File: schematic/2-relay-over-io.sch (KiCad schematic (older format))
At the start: 26 parts, among them J1 Screw_Terminal_01x03, J2 Screw_Terminal_01x03, J5 Conn_02x05_Odd_Even, J6 Conn_02x05_Odd_Even, J7 Conn_02x08_Odd_Even, J8 Conn_02x08_Odd_Even, Q2 BC817, Q3 BC817, U2 SONGLE_3V_relay, U3 SONGLE_3V_relay, U6 DizzyBITLogo, U7 DizzyBIT-Layout

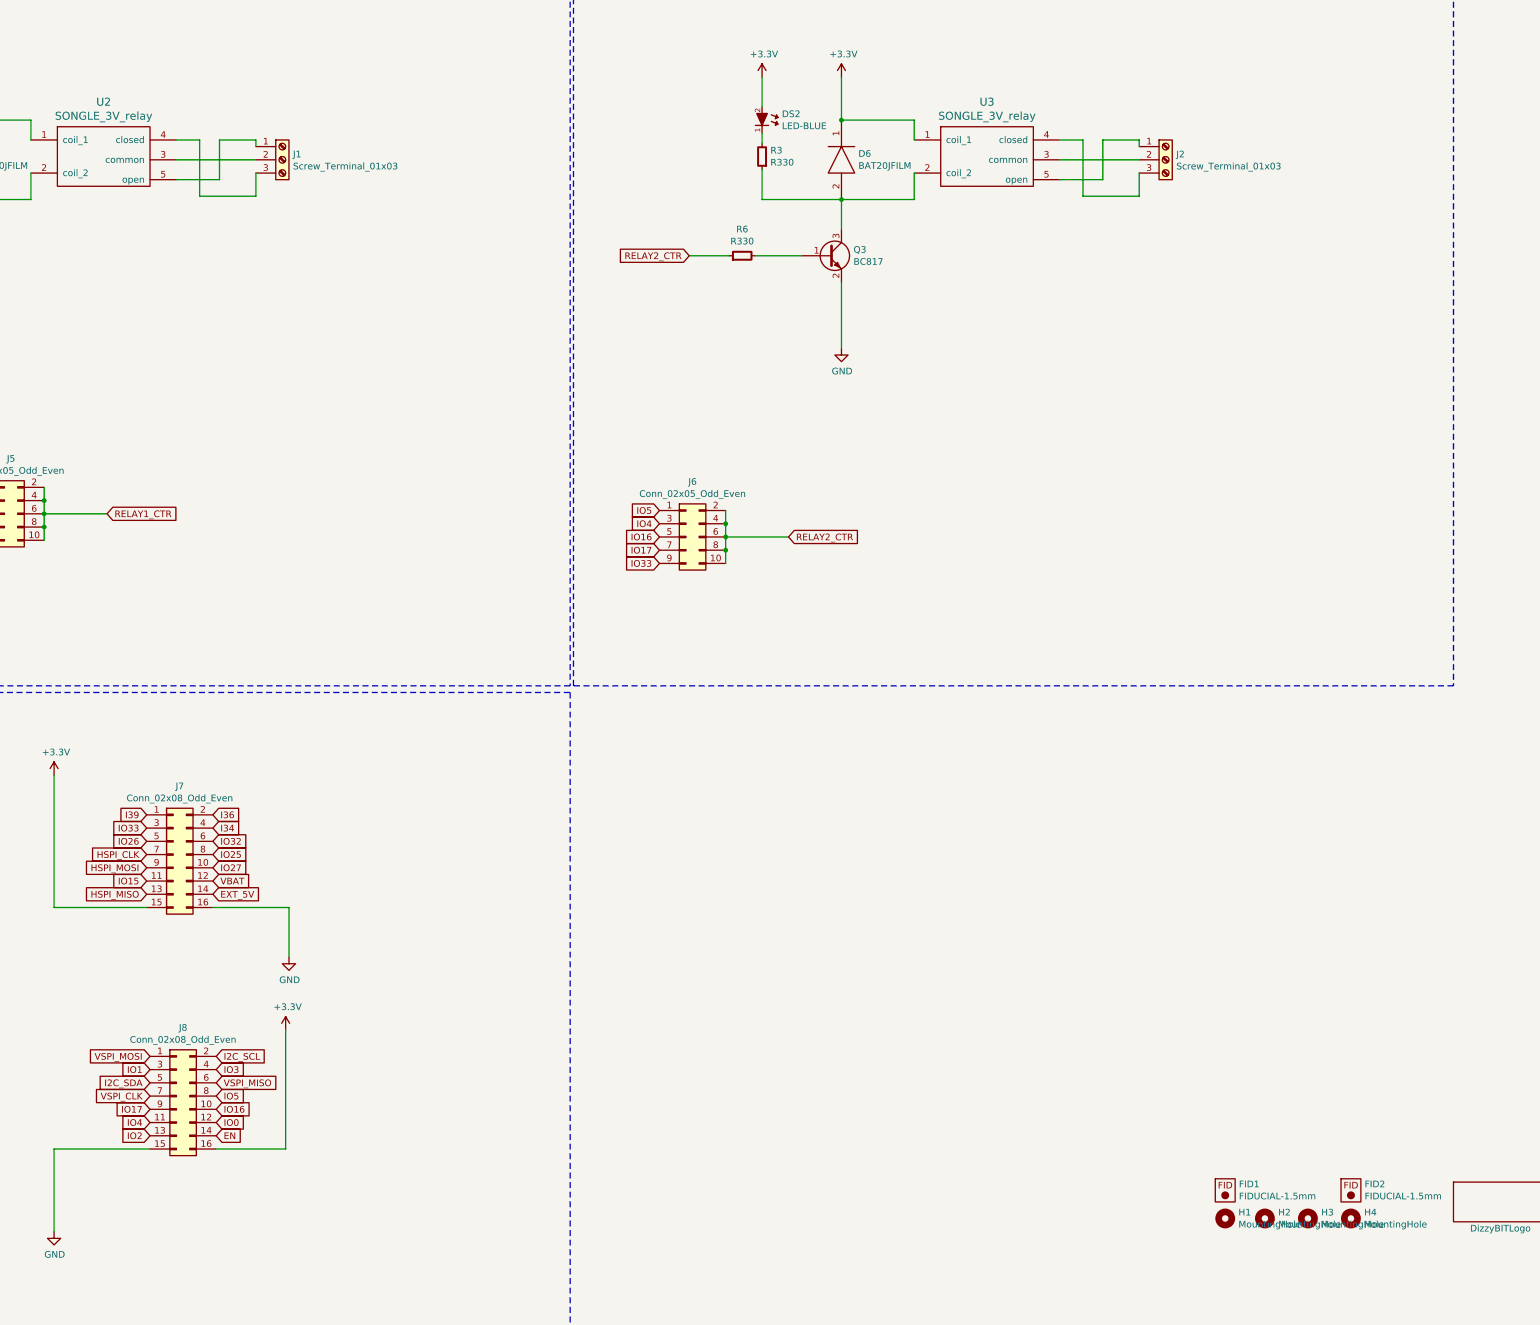
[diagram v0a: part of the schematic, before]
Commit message: Updated according to standard module design
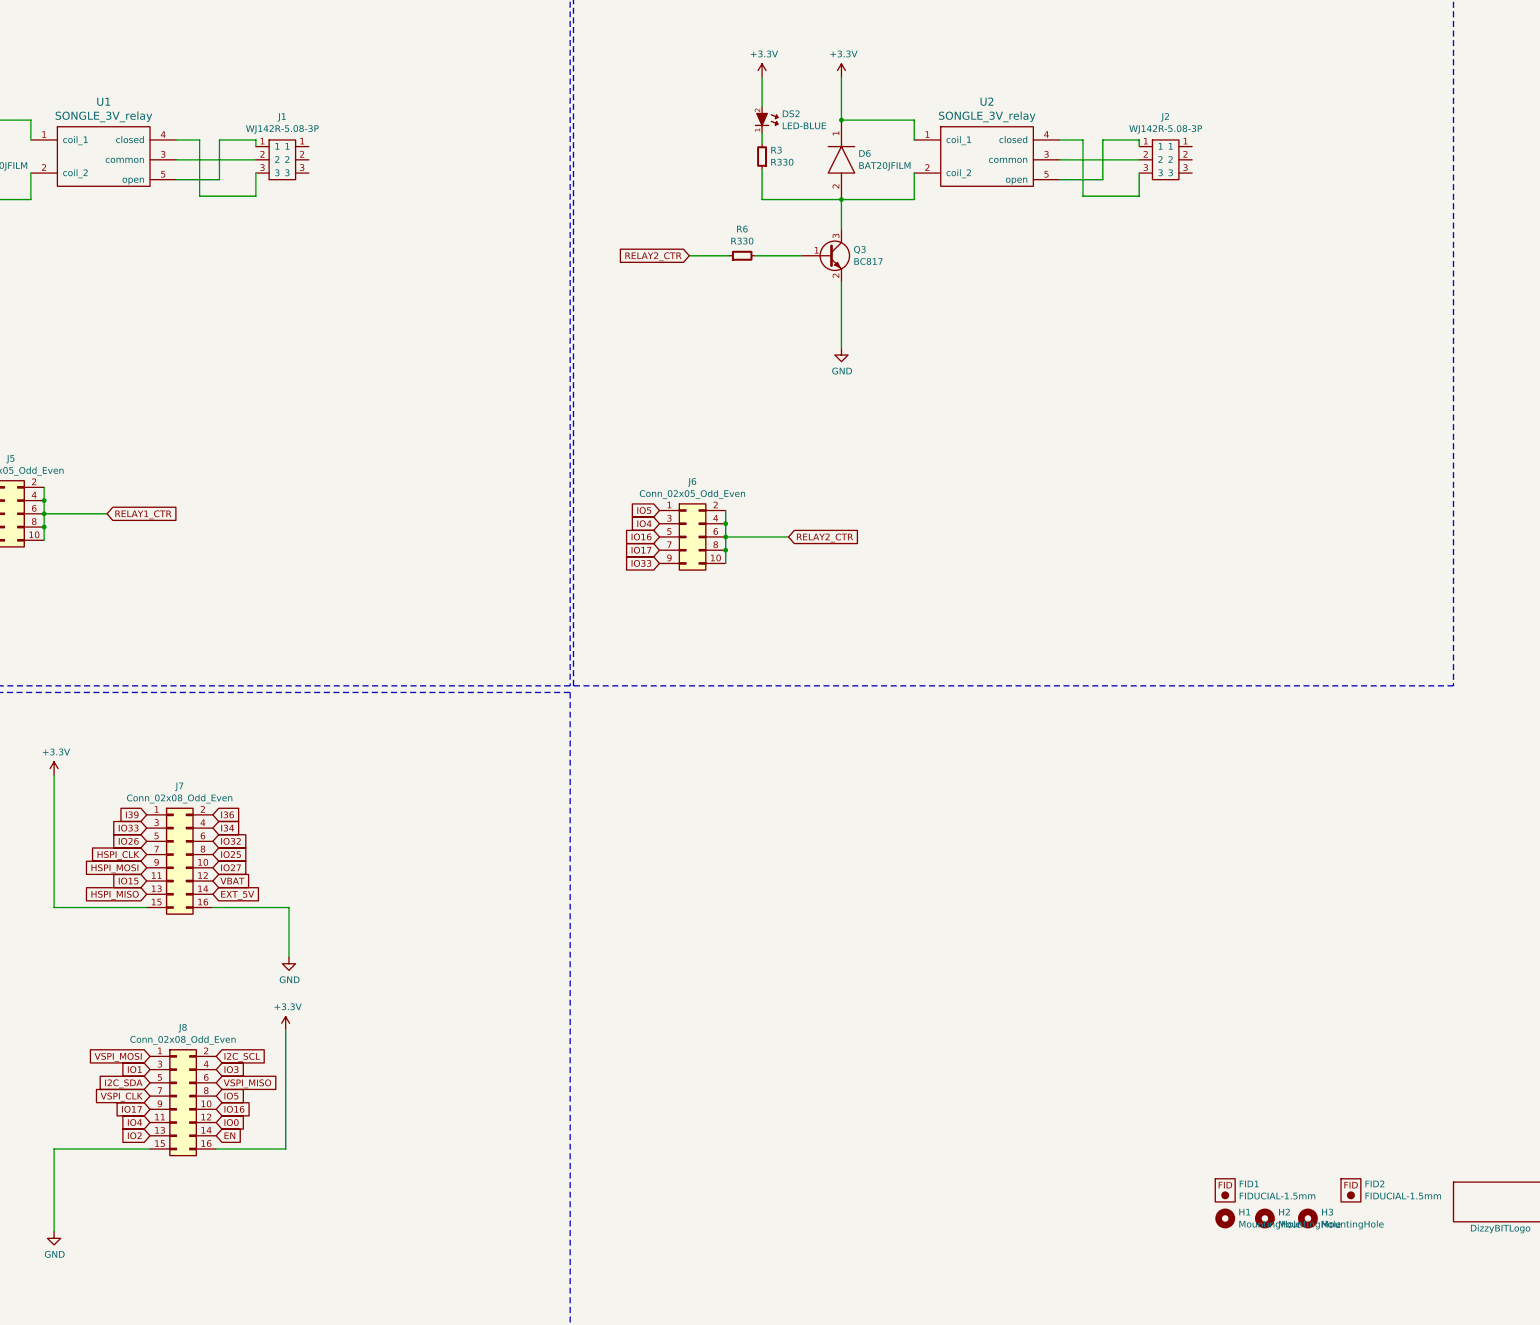
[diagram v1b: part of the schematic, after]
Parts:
- removed H4: MountingHole, MountingHole:MountingHole_2.2mm_M2_DIN965_Pad, symbol Mechanical:MountingHole
- removed J1, J2: Screw_Terminal_01x03, TerminalBlock:TerminalBlock_bornier-3_P5.08mm, symbol Connector:Screw_Terminal_01x03
- added J1, J2: WJ142R-5.08-3P, TerminalBlock:WJ142R-5.08-3P, symbol Connector_Generic:WJ142R-5.08-3P
- renumbered U2 to U1, U3 to U2
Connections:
- net at U1.3 (common): now also J1.2
- net at U1.4 (closed): now also J1.3
- net at U1.5 (open): now also J1.1
- net at U2.3 (common): now also J2.2
- net at U2.4 (closed): now also J2.3
- net at U2.5 (open): now also J2.1
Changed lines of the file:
@@
 EESchema Schematic File Version 4
-LIBS:DizzyBit-1 Relay-cache
+LIBS:2-relay-over-io-cache
 EELAYER 26 0
 EELAYER END
@@
 $EndComp
 $Comp
-L Mechanical:MountingHole H4
-U 1 1 5C8FAF19
-P 13150 10350
-F 0 "H4" H 13250 10396 50  0000 L CNN
-F 1 "MountingHole" H 13250 10305 50  0000 L CNN
-F 2 "MountingHole:MountingHole_2.2mm_M2_DIN965_Pad" H 13150 10350 50  0001 C CNN
-F 3 "~" H 13150 10350 50  0001 C CNN
-	1    13150 10350
-	1    0    0    -1
-$EndComp
-$Comp
 L Mechanical:MountingHole H1
 U 1 1 5C902F86
@@
 $EndComp
 $Comp
-L songle_5v_relay:SONGLE_5V_relay U2
+L songle_5v_relay:SONGLE_5V_relay U1
 U 1 1 5C5C29D5
 P 3725 2350
-F 0 "U2" H 3725 2787 60  0000 C CNN
+F 0 "U1" H 3725 2787 60  0000 C CNN
 F 1 "SONGLE_3V_relay" H 3725 2681 60  0000 C CNN
 F 2 "Songle:SONGLE_5V_Relay" H 3875 2350 60  0001 C CNN
@@
 	1    1875 3075
 	0    -1   -1   0
-$EndComp
-$Comp
-L Connector:Screw_Terminal_01x03 J1
-U 1 1 5C5CB654
-P 5075 2350
-F 0 "J1" H 5155 2392 50  0000 L CNN
-F 1 "Screw_Terminal_01x03" H 5155 2301 50  0000 L CNN
-F 2 "TerminalBlock:TerminalBlock_bornier-3_P5.08mm" H 5075 2350 50  0001 C CNN
-F 3 "" H 5075 2350 50  0001 C CNN
-	1    5075 2350
-	1    0    0    -1
 $EndComp
 Wire Wire Line
@@
 $EndComp
 $Comp
-L songle_5v_relay:SONGLE_5V_relay U3
+L songle_5v_relay:SONGLE_5V_relay U2
 U 1 1 5D9507B5
 P 10400 2350
-F 0 "U3" H 10400 2787 60  0000 C CNN
+F 0 "U2" H 10400 2787 60  0000 C CNN
 F 1 "SONGLE_3V_relay" H 10400 2681 60  0000 C CNN
 F 2 "Songle:SONGLE_5V_Relay" H 10550 2350 60  0001 C CNN
@@
 	0    -1   -1   0
 $EndComp
-$Comp
-L Connector:Screw_Terminal_01x03 J2
-U 1 1 5D9507FF
-P 11750 2350
-F 0 "J2" H 11830 2392 50  0000 L CNN
-F 1 "Screw_Terminal_01x03" H 11830 2301 50  0000 L CNN
-F 2 "TerminalBlock:TerminalBlock_bornier-3_P5.08mm" H 11750 2350 50  0001 C CNN
-F 3 "" H 11750 2350 50  0001 C CNN
-	1    11750 2350
-	1    0    0    -1
-$EndComp
 Wire Wire Line
 	11550 2350 10950 2350
@@
 Text GLabel 7925 5400 0    50   Input ~ 0
 IO33
+$Comp
+L Connector_Generic:WJ142R-5.08-3P J1
+U 1 1 5D93C8FC
+P 4975 2150
+F 0 "J1" H 5075 2275 50  0000 C CNN
+F 1 "WJ142R-5.08-3P" H 5075 2184 50  0000 C CNN
+F 2 "TerminalBlock:WJ142R-5.08-3P" H 4975 2150 50  0001 C CNN
+F 3 "" H 4975 2150 50  0001 C CNN
+	1    4975 2150
+	1    0    0    -1
+$EndComp
+$Comp
+L Connector_Generic:WJ142R-5.08-3P J2
+U 1 1 5D93CB98
+P 11650 2150
+F 0 "J2" H 11750 2275 50  0000 C CNN
+F 1 "WJ142R-5.08-3P" H 11750 2184 50  0000 C CNN
+F 2 "TerminalBlock:WJ142R-5.08-3P" H 11650 2150 50  0001 C CNN
+F 3 "" H 11650 2150 50  0001 C CNN
+	1    11650 2150
+	1    0    0    -1
+$EndComp
 $EndSCHEMATC

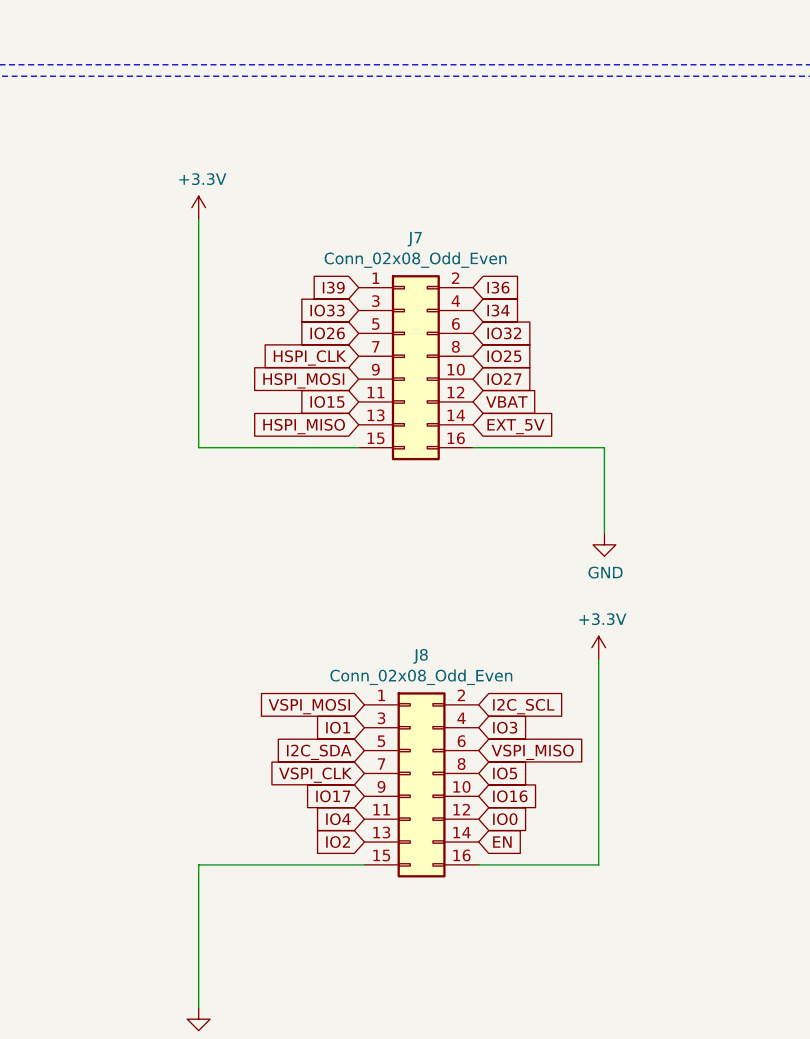
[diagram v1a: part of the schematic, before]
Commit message: Updated 3.3v position and tracks
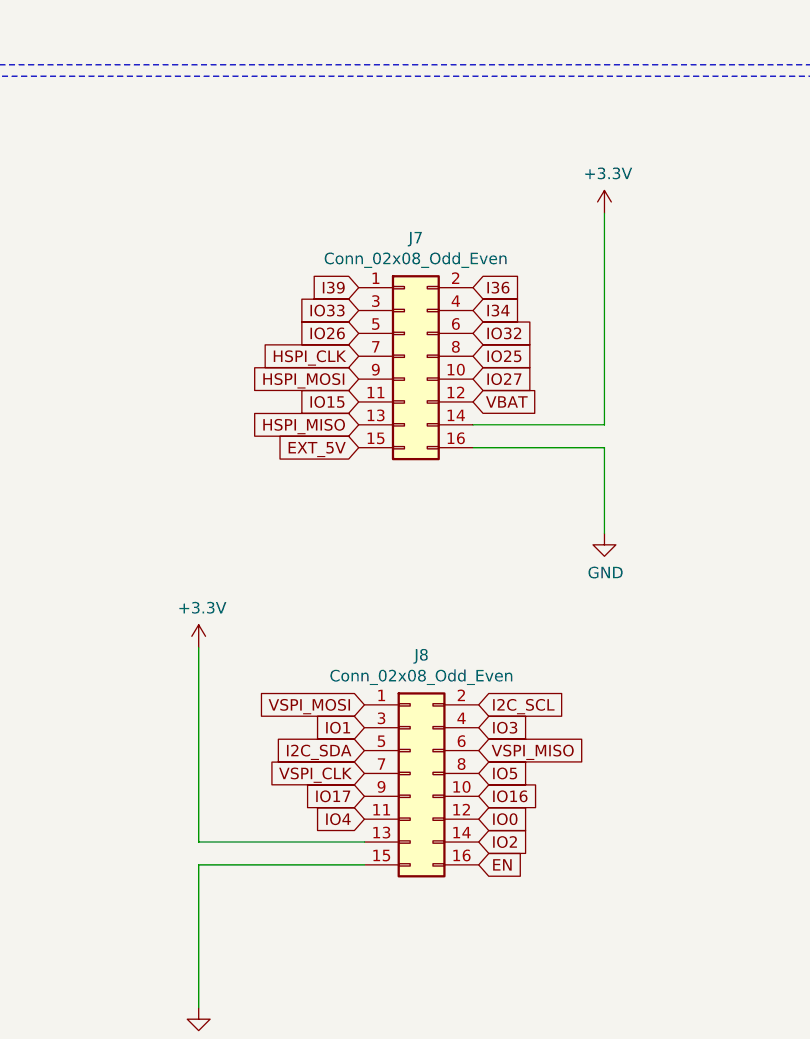
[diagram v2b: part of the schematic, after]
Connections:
- net +3V3: now also J7.14 (Pin_14), J8.13 (Pin_13); no longer J7.15 (Pin_15), J8.16 (Pin_16)
- net EN: now also J8.16 (Pin_16); no longer J8.14 (Pin_14)
- net EXT_5V: now also J7.15 (Pin_15); no longer J7.14 (Pin_14)
- net IO2: now also J8.14 (Pin_14); no longer J8.13 (Pin_13)
- net at J2.1: now also U2.5 (open)
- net at J2.2: now also U2.3 (common)
- net at J2.3: now also U2.4 (closed)
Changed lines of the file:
@@
 L power:+3.3V #PWR0101
 U 1 1 5D8B5B52
-P 3350 7000
-F 0 "#PWR0101" H 3350 6850 50  0001 C CNN
-F 1 "+3.3V" H 3365 7173 50  0000 C CNN
-F 2 "" H 3350 7000 50  0001 C CNN
-F 3 "" H 3350 7000 50  0001 C CNN
-	1    3350 7000
-	1    0    0    -1
-$EndComp
-Wire Wire Line
-	3350 8000 4050 8000
+P 5125 6975
+F 0 "#PWR0101" H 5125 6825 50  0001 C CNN
+F 1 "+3.3V" H 5140 7148 50  0000 C CNN
+F 2 "" H 5125 6975 50  0001 C CNN
+F 3 "" H 5125 6975 50  0001 C CNN
+	1    5125 6975
+	1    0    0    -1
+$EndComp
 $Comp
 L power:GND #PWR0102
@@
 L power:+3.3V #PWR0103
 U 1 1 5D8B5BF6
-P 5100 8925
-F 0 "#PWR0103" H 5100 8775 50  0001 C CNN
-F 1 "+3.3V" H 5115 9098 50  0000 C CNN
-F 2 "" H 5100 8925 50  0001 C CNN
-F 3 "" H 5100 8925 50  0001 C CNN
-	1    5100 8925
+P 3350 8875
+F 0 "#PWR0103" H 3350 8725 50  0001 C CNN
+F 1 "+3.3V" H 3365 9048 50  0000 C CNN
+F 2 "" H 3350 8875 50  0001 C CNN
+F 3 "" H 3350 8875 50  0001 C CNN
+	1    3350 8875
 	1    0    0    -1
 $EndComp
@@
 $EndComp
 Wire Wire Line
-	4575 9825 5100 9825
-Wire Wire Line
-	5100 9825 5100 8925
-Wire Wire Line
 	5125 8375 5125 8000
-Wire Wire Line
-	3350 8000 3350 7000
 Text GLabel 4075 9325 0    50   Input ~ 0
 I2C_SDA
@@
 Text GLabel 4075 9225 0    50   Input ~ 0
 IO1
-Text GLabel 4075 9725 0    50   Input ~ 0
+Text GLabel 4575 9725 2    50   Input ~ 0
 IO2
 Text GLabel 4575 9225 2    50   Input ~ 0
@@
 Text GLabel 4050 7300 0    50   Input ~ 0
 I39
-Text GLabel 4550 7900 2    50   Input ~ 0
+Text GLabel 4050 8000 0    50   Input ~ 0
 EXT_5V
 Wire Notes Line
@@
 Text GLabel 4550 7800 2    50   Input ~ 0
 VBAT
-Text GLabel 4575 9725 2    50   Input ~ 0
+Text GLabel 4575 9825 2    50   Input ~ 0
 EN
 $Comp
@@
 	1    0    0    -1
 $EndComp
+Wire Wire Line
+	4075 9725 3350 9725
+Wire Wire Line
+	3350 9725 3350 8875
+Wire Wire Line
+	5125 6975 5125 7900
+Wire Wire Line
+	5125 7900 4550 7900
 $EndSCHEMATC
